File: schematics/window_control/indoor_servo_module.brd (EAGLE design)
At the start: 48.2 x 59.4 mm, 29 parts, among them J1 MTR-SERVO-FS5103B, J2 JST-XH2.54-4P, J3 JST-XH2.54-2P, J4 JST-XH2.54-3P, Q2 2N3904, Q3 2N3906BU, Q4 2N3904, Q5 STP14NM50N, SW1 SWITCH, U2 LM311P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

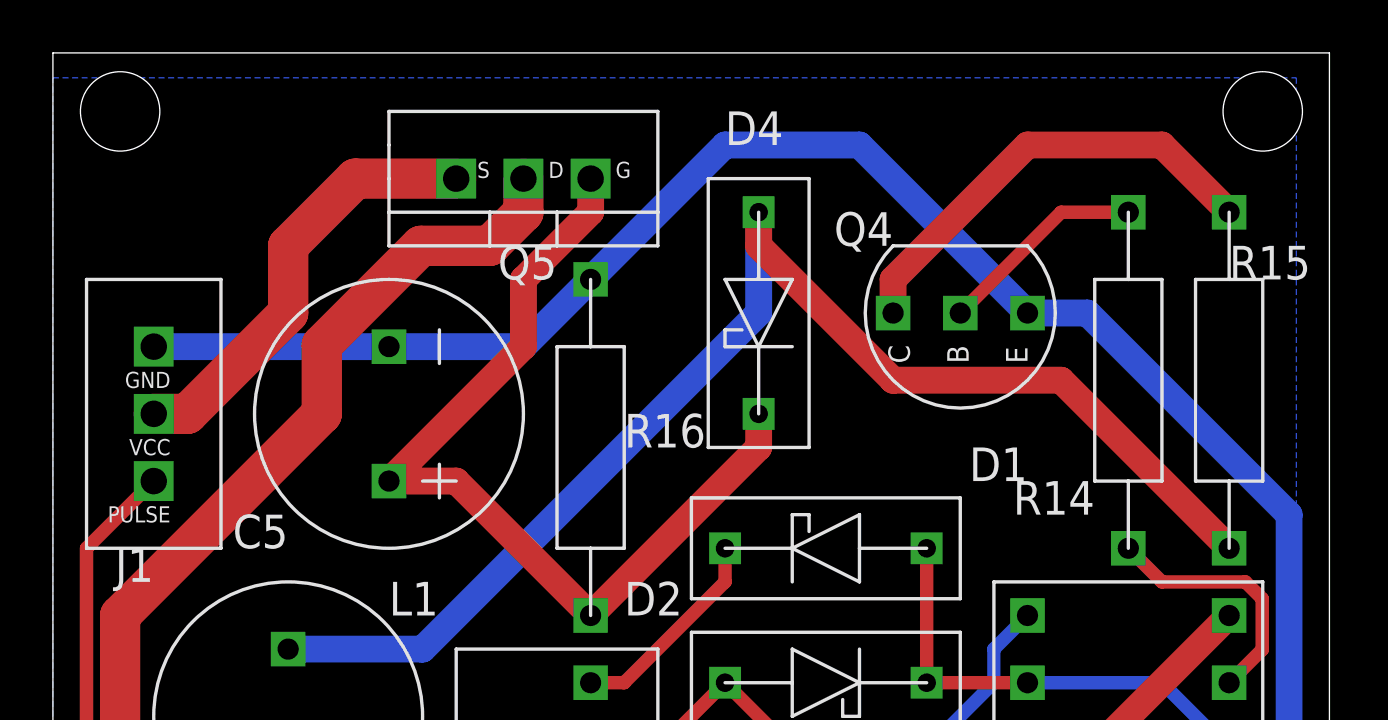
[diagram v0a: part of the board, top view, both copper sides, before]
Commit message: Holes moved away from board border
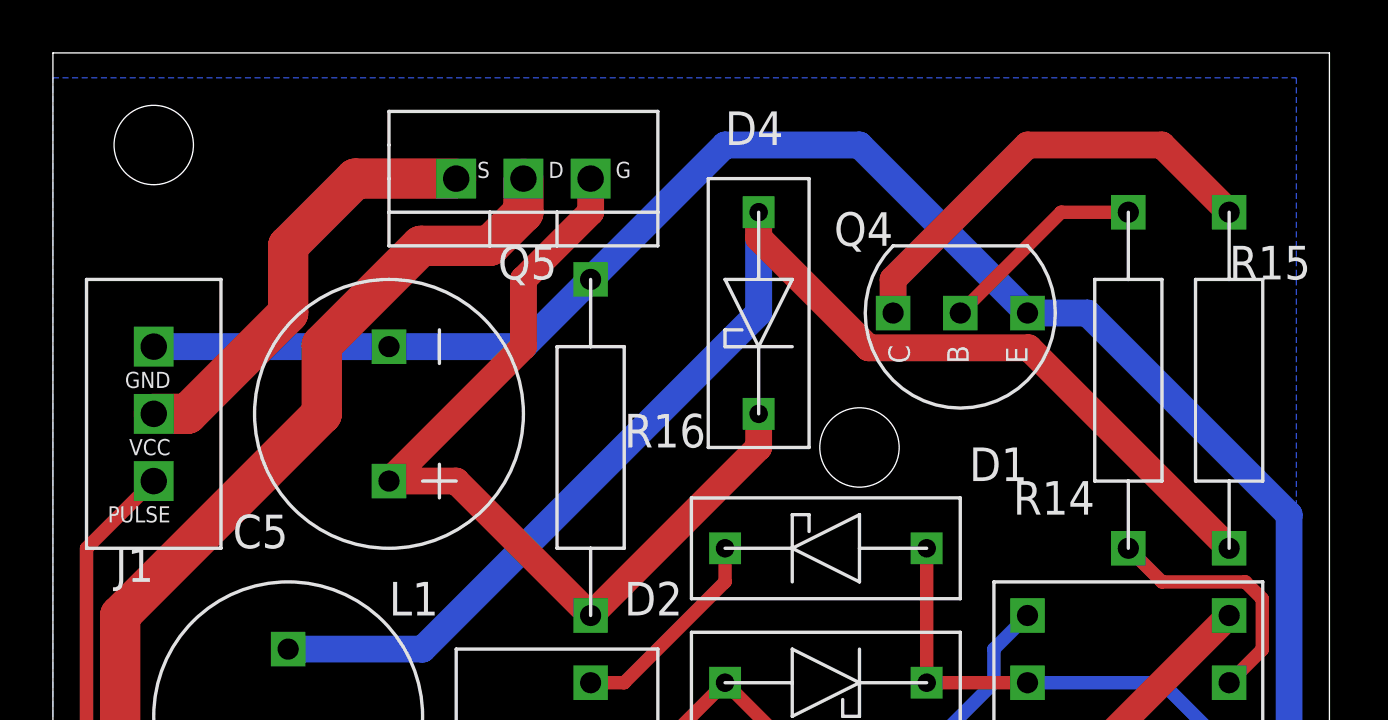
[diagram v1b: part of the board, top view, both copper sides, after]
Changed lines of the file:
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@@
 <wire x1="85.07" y1="50.47" x2="36.83" y2="50.47" width="0" layer="20"/>
 <wire x1="36.83" y1="50.47" x2="36.83" y2="-8.89" width="0" layer="20"/>
-<hole x="39.37" y="48.26" drill="3"/>
-<hole x="82.55" y="48.26" drill="3"/>
+<hole x="40.64" y="46.99" drill="3"/>
+<hole x="67.31" y="35.56" drill="3"/>
 <hole x="63.5" y="6.35" drill="3"/>
 <text x="54.61" y="-7.62" size="1.778" layer="26" rot="MR0">GND</text>
@@
 <contactref element="R15" pad="P$2"/>
 <wire x1="45.72" y1="27.94" x2="50.8" y2="27.94" width="1.016" layer="16"/>
-<wire x1="74.93" y1="38.1" x2="68.58" y2="38.1" width="1.016" layer="1"/>
-<wire x1="68.58" y1="38.1" x2="63.5" y2="43.18" width="1.016" layer="1"/>
-<wire x1="63.5" y1="43.18" x2="63.5" y2="44.45" width="1.016" layer="1"/>
-<wire x1="81.28" y1="31.75" x2="74.93" y2="38.1" width="1.016" layer="1"/>
+<wire x1="50.8" y1="27.94" x2="63.5" y2="40.64" width="1.016" layer="16"/>
+<wire x1="73.7044" y1="39.3256" x2="67.65245625" y2="39.3256" width="1.016" layer="1"/>
+<wire x1="81.28" y1="31.75" x2="73.7044" y2="39.3256" width="1.016" layer="1"/>
+<wire x1="67.65245625" y1="39.3256" x2="63.5" y2="43.47805625" width="1.016" layer="1"/>
+<wire x1="63.5" y1="43.47805625" x2="63.5" y2="44.45" width="1.016" layer="1"/>
 <wire x1="63.5" y1="40.64" x2="63.5" y2="44.45" width="1.016" layer="16"/>
-<wire x1="50.8" y1="27.94" x2="63.5" y2="40.64" width="1.016" layer="16"/>
 </signal>
 <signal name="N$40">
